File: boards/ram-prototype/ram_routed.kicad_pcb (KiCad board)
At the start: 4 copper layers, 159 x 77 mm, 512 parts, among them J1 PinHeader_1x16_P2\.54mm_Verti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, U1 DSBGA\-5_NumericPads, U10 DSBGA\-6_NumericPads, U100 DSBGA\-5_NumericPads, U101 DSBGA\-5_NumericPads, U102 DSBGA\-5_NumericPads, U103 DSBGA\-5_NumericPads, U104 DSBGA\-5_NumericPads, U105 DSBGA\-5_NumericPads, U106 DSBGA\-5_NumericPads, U107 DSBGA\-5_NumericPads, U108 DSBGA\-5_NumericPads, U109 DSBGA\-5_NumericPads, U11 DSBGA\-6_NumericPads, U110 DSBGA\-5_NumericPads, U111 DSBGA\-5_NumericPads, U112 DSBGA\-5_NumericPads, U113 DSBGA\-5_NumericPads, U114 DSBGA\-5_NumericPads, U115 DSBGA\-5_NumericPads, U116 DSBGA\-5_NumericPads, U117 DSBGA\-5_NumericPads, U118 DSBGA\-5_NumericPads, U119 DSBGA\-5_NumericPads, U12 DSBGA\-5_NumericPads, U120 DSBGA\-5_NumericPads, U121 DSBGA\-5_NumericPads, U122 DSBGA\-5_NumericPads, U123 DSBGA\-5_NumericPads, U124 DSBGA\-5_NumericPads, U125 DSBGA\-5_NumericPads, U126 DSBGA\-5_NumericPads, U127 DSBGA\-5_NumericPads, U128 DSBGA\-5_NumericPads, U129 DSBGA\-5_NumericPads, U13 DSBGA\-5_NumericPads, U130 DSBGA\-5_NumericPads, U131 DSBGA\-5_NumericPads, U132 DSBGA\-5_NumericPads, U133 DSBGA\-5_NumericPads, U134 DSBGA\-5_NumericPads, U135 DSBGA\-5_NumericPads, U136 DSBGA\-5_NumericPads, U137 DSBGA\-5_NumericPads, U138 DSBGA\-5_NumericPads, U139 DSBGA\-5_NumericPads, U14 DSBGA\-5_NumericPads, U140 DSBGA\-5_NumericPads, U141 DSBGA\-5_NumericPads, U142 DSBGA\-5_NumericPads, U143 DSBGA\-5_NumericPads, U144 DSBGA\-5_NumericPads, U145 DSBGA\-5_NumericPads, U146 DSBGA\-5_NumericPads, U147 DSBGA\-5_NumericPads, U148 DSBGA\-5_NumericPads, U149 DSBGA\-5_NumericPads, U15 DSBGA\-5_NumericPads, U150 DSBGA\-5_NumericPads, U151 DSBGA\-5_NumericPads, U152 DSBGA\-5_NumericPads, U153 DSBGA\-5_NumericPads, U154 DSBGA\-5_NumericPads, U155 DSBGA\-5_NumericPads, U156 DSBGA\-5_NumericPads, U157 DSBGA\-5_NumericPads, U158 DSBGA\-5_NumericPads, U159 DSBGA\-5_NumericPads, U16 DSBGA\-5_NumericPads, U160 DSBGA\-5_NumericPads, U161 DSBGA\-5_NumericPads, U17 DSBGA\-5_NumericPads, U18 DSBGA\-5_NumericPads, U19 DSBGA\-5_NumericPads, U2 DSBGA\-5_NumericPads, U20 DSBGA\-5_NumericPads, U21 DSBGA\-5_NumericPads, U22 DSBGA\-5_NumericPads, U23 DSBGA\-5_NumericPads, U24 DSBGA\-5_NumericPads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

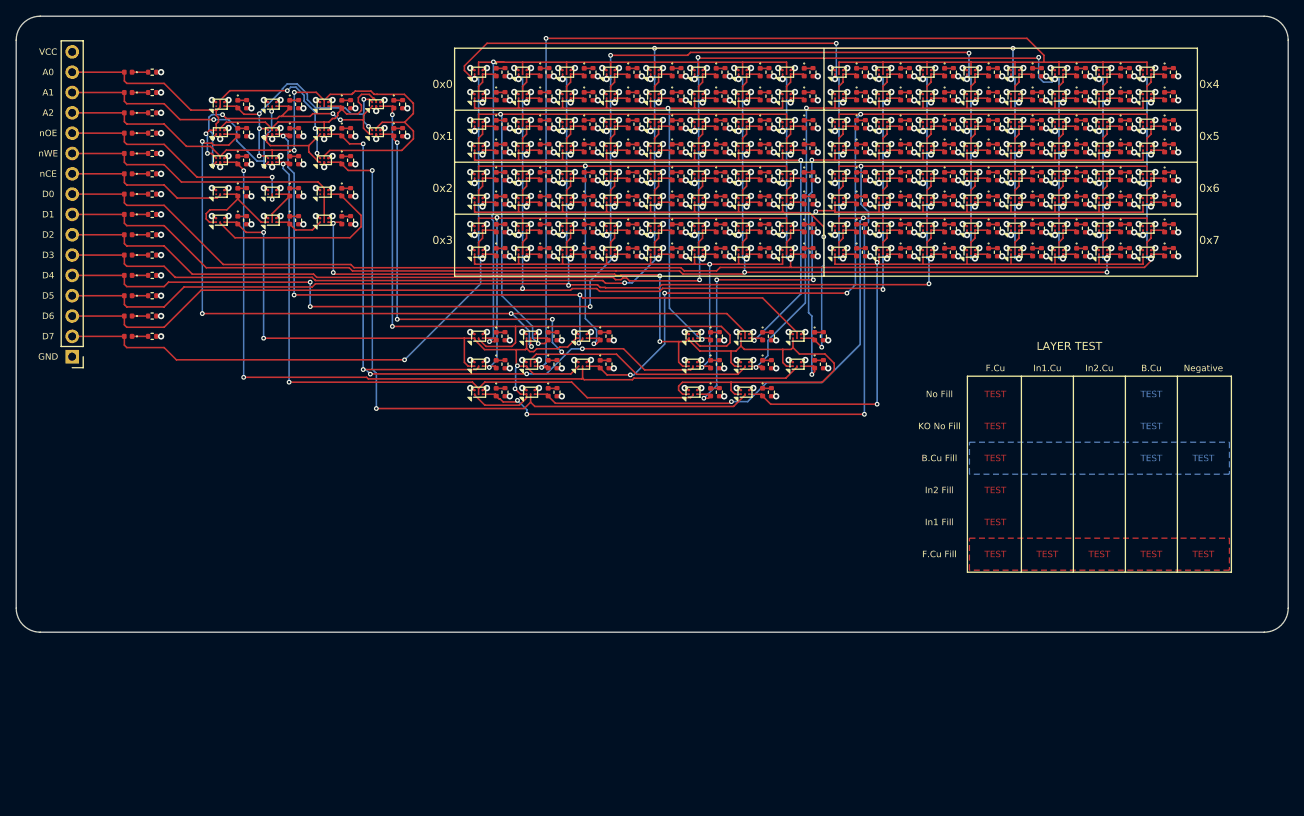
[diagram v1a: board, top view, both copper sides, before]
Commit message: flip resistor to the back
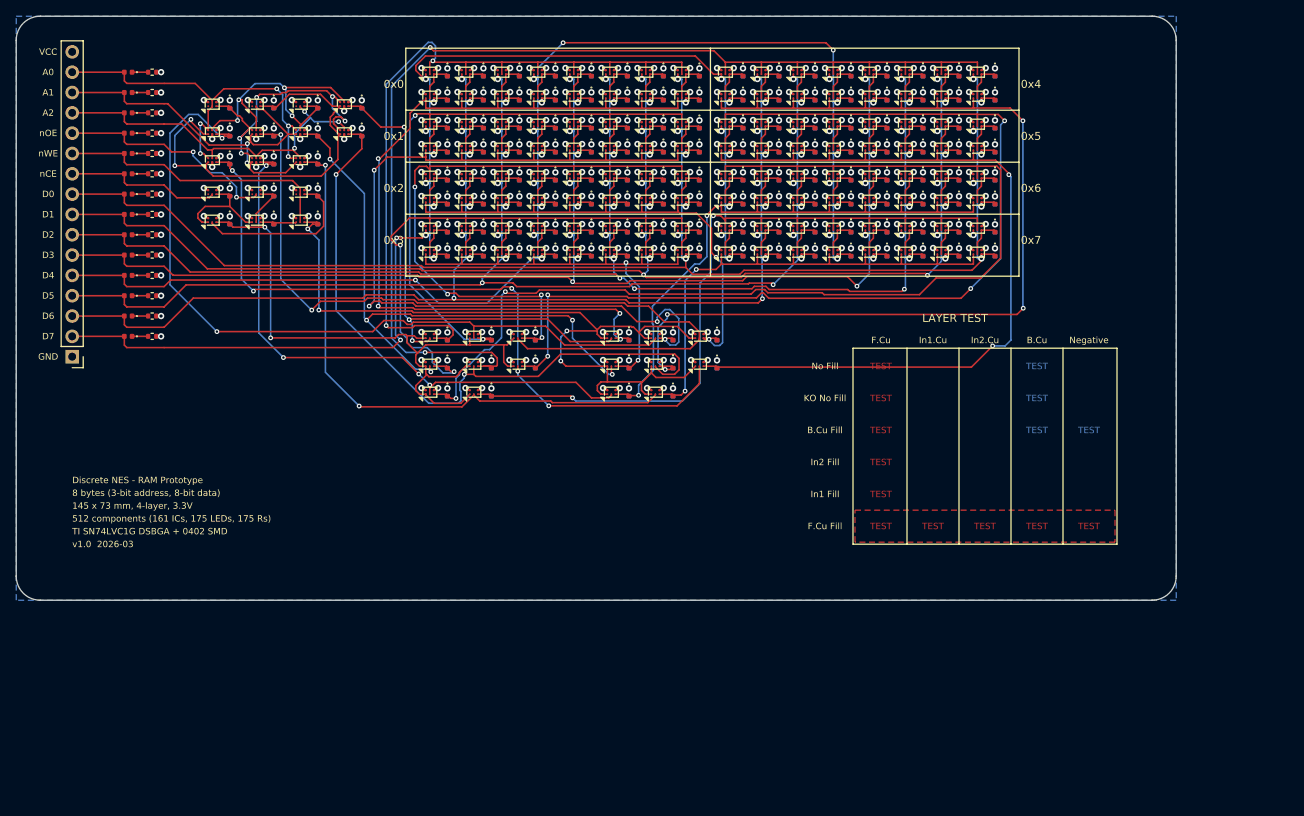
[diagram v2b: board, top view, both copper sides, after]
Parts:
- R100, R101, R102, R103, R104, R105, R106, R107, R108, R109, R110, R111, R112, R113, R114, R115, R116, R117, R118, R119, R120, R121, R122, R123, R124, R125, R126, R127, R128, R129, R130, R131, R132, R133, R134, R135, R136, R137, R138, R139, R140, R141, R142, R143, R144, R145, R146, R147, R148, R149, R15, R150, R151, R152, R153, R154, R155, R156, R157, R158, R159, R16, R160, R161, R162, R163, R164, R165, R166, R167, R168, R169, R17, R170, R171, R172, R173, R174, R175, R18, R19, R20, R21, R22, R23, R24, R25, R26, R27, R28, R29, R30, R31, R32, R33, R34, R35, R36, R37, R38, R39, R40, R41, R42, R43, R44, R45, R46, R47, R48, R49, R50, R51, R52, R53, R54, R55, R56, R57, R58, R59, R60, R61, R62, R63, R64, R65, R66, R67, R68, R69, R70, R71, R72, R73, R74, R75, R76, R77, R78, R79, R80, R81, R82, R83, R84, R85, R86, R87, R88, R89, R90, R91, R92, R93, R94, R95, R96, R97, R98, R99: moved to B.Cu
- moved R52 22.3 mm to (135.3, 20.0)
- moved R53 22.3 mm to (135.3, 26.5)
- moved R54 22.3 mm to (135.3, 33.0)
- moved R55 22.3 mm to (135.3, 39.5)
- moved R60 22.3 mm to (135.3, 23.0)
- moved R61 22.3 mm to (135.3, 29.5)
- moved R62 22.3 mm to (135.3, 36.0)
- moved R63 22.3 mm to (135.3, 42.5)
- moved R68 21.3 mm to (130.8, 20.0)
- moved R69 21.3 mm to (130.8, 26.5)
- moved R70 21.3 mm to (130.8, 33.0)
- moved R71 21.3 mm to (130.8, 39.5)
- moved R76 21.3 mm to (130.8, 23.0)
- moved R77 21.3 mm to (130.8, 29.5)
- moved R78 21.3 mm to (130.8, 36.0)
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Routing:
- net GND: track 202.2 -> 105.6 mm, vias 336 -> 175
- net /BUF_OE_4: track 89.8 -> 127.2 mm, vias 2 -> 4
- net /BUF_OE_1: track 78.1 -> 114.4 mm, vias 2 -> 4
- net /Address Decoder/A2: track 78.4 -> 45.6 mm, vias 2 -> 3
- net /BUF_OE_5: track 81.3 -> 107.6 mm
- net /BUF_OE_0: track 81.4 -> 106.7 mm, vias 2 -> 4
- net /Byte 5/WRITE_CLK: track 114.6 -> 135.7 mm
- net /Address Decoder/SEL0: track 85.5 -> 64.5 mm, vias 2 -> 3
- net /D0: track 218.3 -> 197.4 mm
- net /D3: track 205.8 -> 185.0 mm, vias 19 -> 18
- net /D4: track 204.5 -> 183.7 mm, vias 21 -> 19
- net /D1: track 213.5 -> 193.1 mm
- net /Byte 4/WRITE_CLK: track 158.5 -> 138.2 mm
- net /D2: track 211.7 -> 191.5 mm
- net /BUF_OE_7: track 83.1 -> 64.3 mm
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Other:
- board size 159 x 77 mm -> 145 x 73 mm
- board text added: "145 x 73 mm, 4-layer, 3.3V"
- board text added: "512 components (161 ICs, 175 LEDs, 175 Rs)"
- board text added: "8 bytes (3-bit address, 8-bit data)"
- board text added: "Discrete NES - RAM Prototype"
- board text added: "TI SN74LVC1G DSBGA + 0402 SMD"
- board text added: "v1.0 2026-03"

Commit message: Fix some layer issues
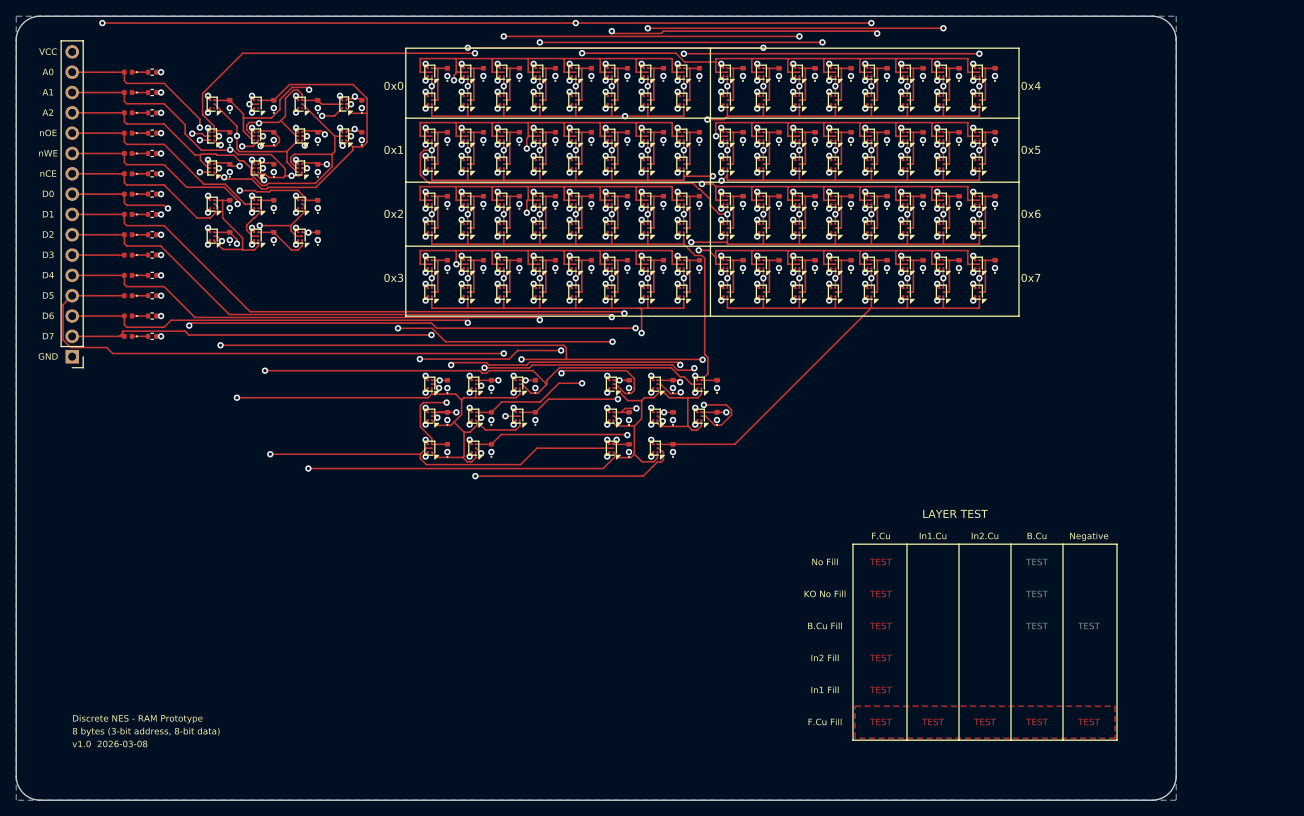
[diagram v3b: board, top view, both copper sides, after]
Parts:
- removed D112, D113, D114, D115, D116, D117, D118, D119, D120, D121, D122, D123, D124, D125, D126, D127, D128, D129, D130, D131, D132, D133, D134, D135, D136, D137, D138, D139, D140, D141, D142, D143, D144, D145, D146, D147, D148, D149, D150, D151, D152, D153, D154, D155, D156, D157, D158, D159, D160, D161, D162, D163, D164, D165, D166, D167, D168, D169, D170, D171, D172, D173, D174, D175: LED_0402_1005Metric, LED_SMD:LED_0402_1005Metric
- removed R112, R113, R114, R115, R116, R117, R118, R119, R120, R121, R122, R123, R124, R125, R126, R127, R128, R129, R130, R131, R132, R133, R134, R135, R136, R137, R138, R139, R140, R141, R142, R143, R144, R145, R146, R147, R148, R149, R150, R151, R152, R153, R154, R155, R156, R157, R158, R159, R160, R161, R162, R163, R164, R165, R166, R167, R168, R169, R170, R171, R172, R173, R174, R175: R_0402_1005Metric, Resistor_SMD:R_0402_1005Metric
- J1: moved to B.Cu
- moved D104 18.2 mm to (66.9, 20.0), turned to 90 degrees
- moved D108 18.2 mm to (103.8, 20.0), turned to 90 degrees
- moved R104 18.2 mm to (66.9, 20.0), turned to 90 degrees
- moved R108 18.2 mm to (103.8, 20.0), turned to 90 degrees
- moved D105 18.1 mm to (66.9, 28.0), turned to 90 degrees
- moved D107 18.1 mm to (66.9, 44.0), turned to 90 degrees
- moved D109 18.1 mm to (103.8, 28.0), turned to 90 degrees
- moved D111 18.1 mm to (103.8, 44.0), turned to 90 degrees
- moved R105 18.1 mm to (66.9, 28.0), turned to 90 degrees
- moved R107 18.1 mm to (66.9, 44.0), turned to 90 degrees
- moved R109 18.1 mm to (103.8, 28.0), turned to 90 degrees
- moved R111 18.1 mm to (103.8, 44.0), turned to 90 degrees
- moved D106 18.0 mm to (66.9, 36.0), turned to 90 degrees
- moved D110 18.0 mm to (103.8, 36.0), turned to 90 degrees
- moved R106 18.0 mm to (66.9, 36.0), turned to 90 degrees
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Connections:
- D104 pad 2: /D3 -> Net-(D104-A)
- D105 pad 2: /D3 -> Net-(D105-A)
- D106 pad 2: /D3 -> Net-(D106-A)
- D107 pad 2: /D3 -> Net-(D107-A)
- D108 pad 2: /D3 -> Net-(D108-A)
- D109 pad 2: /D3 -> Net-(D109-A)
- D110 pad 2: /D3 -> Net-(D110-A)
- D111 pad 2: /D3 -> Net-(D111-A)
- D56 pad 2: /D0 -> Net-(D56-A)
- D57 pad 2: /D0 -> Net-(D57-A)
- D58 pad 2: /D0 -> Net-(D58-A)
- D59 pad 2: /D0 -> Net-(D59-A)
- D60 pad 2: /D0 -> Net-(D60-A)
- D61 pad 2: /D0 -> Net-(D61-A)
- D62 pad 2: /D0 -> Net-(D62-A)
- D63 pad 2: /D0 -> Net-(D63-A)
- D72 pad 2: /D1 -> Net-(D72-A)
- D73 pad 2: /D1 -> Net-(D73-A)
- D74 pad 2: /D1 -> Net-(D74-A)
- D75 pad 2: /D1 -> Net-(D75-A)
- D76 pad 2: /D1 -> Net-(D76-A)
- D77 pad 2: /D1 -> Net-(D77-A)
- D78 pad 2: /D1 -> Net-(D78-A)
- D79 pad 2: /D1 -> Net-(D79-A)
- D88 pad 2: /D2 -> Net-(D88-A)
- D89 pad 2: /D2 -> Net-(D89-A)
- D90 pad 2: /D2 -> Net-(D90-A)
- D91 pad 2: /D2 -> Net-(D91-A)
- D92 pad 2: /D2 -> Net-(D92-A)
- D93 pad 2: /D2 -> Net-(D93-A)
- D94 pad 2: /D2 -> Net-(D94-A)
- D95 pad 2: /D2 -> Net-(D95-A)
- U100 pad 4: Net-(D114-A) -> Net-(D82-A)
- U101 pad 4: Net-(D115-A) -> Net-(D83-A)
- U102 pad 4: Net-(D116-A) -> Net-(D84-A)
- U103 pad 4: Net-(D117-A) -> Net-(D85-A)
- U104 pad 4: Net-(D118-A) -> Net-(D86-A)
- U105 pad 4: Net-(D119-A) -> Net-(D87-A)
- U106 pad 2: Net-(D112-A) -> Net-(D80-A)
- U107 pad 2: Net-(D113-A) -> Net-(D81-A)
- U108 pad 2: Net-(D114-A) -> Net-(D82-A)
- U109 pad 2: Net-(D115-A) -> Net-(D83-A)
- U110 pad 2: Net-(D116-A) -> Net-(D84-A)
- U111 pad 2: Net-(D117-A) -> Net-(D85-A)
- U112 pad 2: Net-(D118-A) -> Net-(D86-A)
- U113 pad 2: Net-(D119-A) -> Net-(D87-A)
- U114 pad 4: Net-(D128-A) -> Net-(D88-A)
- U115 pad 4: Net-(D129-A) -> Net-(D89-A)
- U116 pad 4: Net-(D130-A) -> Net-(D90-A)
- U117 pad 4: Net-(D131-A) -> Net-(D91-A)
- U118 pad 4: Net-(D132-A) -> Net-(D92-A)
- U119 pad 4: Net-(D133-A) -> Net-(D93-A)
- U120 pad 4: Net-(D134-A) -> Net-(D94-A)
- U121 pad 4: Net-(D135-A) -> Net-(D95-A)
- U122 pad 2: Net-(D128-A) -> Net-(D88-A)
- U123 pad 2: Net-(D129-A) -> Net-(D89-A)
- U124 pad 2: Net-(D130-A) -> Net-(D90-A)
- U125 pad 2: Net-(D131-A) -> Net-(D91-A)
- U126 pad 2: Net-(D132-A) -> Net-(D92-A)
- U127 pad 2: Net-(D133-A) -> Net-(D93-A)
- U128 pad 2: Net-(D134-A) -> Net-(D94-A)
- U129 pad 2: Net-(D135-A) -> Net-(D95-A)
- U130 pad 4: Net-(D144-A) -> Net-(D96-A)
- U131 pad 4: Net-(D145-A) -> Net-(D97-A)
- U132 pad 4: Net-(D146-A) -> Net-(D98-A)
- U133 pad 4: Net-(D147-A) -> Net-(D99-A)
- U134 pad 4: Net-(D148-A) -> Net-(D100-A)
- U135 pad 4: Net-(D149-A) -> Net-(D101-A)
- U136 pad 4: Net-(D150-A) -> Net-(D102-A)
- U137 pad 4: Net-(D151-A) -> Net-(D103-A)
- U138 pad 2: Net-(D144-A) -> Net-(D96-A)
- U139 pad 2: Net-(D145-A) -> Net-(D97-A)
- U140 pad 2: Net-(D146-A) -> Net-(D98-A)
- U141 pad 2: Net-(D147-A) -> Net-(D99-A)
- U142 pad 2: Net-(D148-A) -> Net-(D100-A)
- U143 pad 2: Net-(D149-A) -> Net-(D101-A)
- U144 pad 2: Net-(D150-A) -> Net-(D102-A)
- U145 pad 2: Net-(D151-A) -> Net-(D103-A)
- U146 pad 4: Net-(D160-A) -> Net-(D104-A)
- U147 pad 4: Net-(D161-A) -> Net-(D105-A)
- U148 pad 4: Net-(D162-A) -> Net-(D106-A)
- U149 pad 4: Net-(D163-A) -> Net-(D107-A)
- U150 pad 4: Net-(D164-A) -> Net-(D108-A)
- U151 pad 4: Net-(D165-A) -> Net-(D109-A)
- U152 pad 4: Net-(D166-A) -> Net-(D110-A)
- U153 pad 4: Net-(D167-A) -> Net-(D111-A)
- U154 pad 2: Net-(D160-A) -> Net-(D104-A)
- U155 pad 2: Net-(D161-A) -> Net-(D105-A)
- U156 pad 2: Net-(D162-A) -> Net-(D106-A)
- U157 pad 2: Net-(D163-A) -> Net-(D107-A)
- U158 pad 2: Net-(D164-A) -> Net-(D108-A)
- U159 pad 2: Net-(D165-A) -> Net-(D109-A)
- U160 pad 2: Net-(D166-A) -> Net-(D110-A)
- U161 pad 2: Net-(D167-A) -> Net-(D111-A)
- U50 pad 4: Net-(D64-A) -> Net-(D56-A)
- U51 pad 4: Net-(D65-A) -> Net-(D57-A)
- U52 pad 4: Net-(D66-A) -> Net-(D58-A)
- U53 pad 4: Net-(D67-A) -> Net-(D59-A)
- U54 pad 4: Net-(D68-A) -> Net-(D60-A)
- U55 pad 4: Net-(D69-A) -> Net-(D61-A)
- U56 pad 4: Net-(D70-A) -> Net-(D62-A)
- U57 pad 4: Net-(D71-A) -> Net-(D63-A)
- U58 pad 2: Net-(D64-A) -> Net-(D56-A)
- U59 pad 2: Net-(D65-A) -> Net-(D57-A)
- U60 pad 2: Net-(D66-A) -> Net-(D58-A)
- U61 pad 2: Net-(D67-A) -> Net-(D59-A)
- U62 pad 2: Net-(D68-A) -> Net-(D60-A)
- U63 pad 2: Net-(D69-A) -> Net-(D61-A)
- U64 pad 2: Net-(D70-A) -> Net-(D62-A)
- U65 pad 2: Net-(D71-A) -> Net-(D63-A)
- U66 pad 4: Net-(D80-A) -> Net-(D64-A)
- U67 pad 4: Net-(D81-A) -> Net-(D65-A)
- U68 pad 4: Net-(D82-A) -> Net-(D66-A)
- U69 pad 4: Net-(D83-A) -> Net-(D67-A)
- U70 pad 4: Net-(D84-A) -> Net-(D68-A)
- U71 pad 4: Net-(D85-A) -> Net-(D69-A)
- U72 pad 4: Net-(D86-A) -> Net-(D70-A)
- U73 pad 4: Net-(D87-A) -> Net-(D71-A)
- U74 pad 2: Net-(D80-A) -> Net-(D64-A)
- U75 pad 2: Net-(D81-A) -> Net-(D65-A)
- U76 pad 2: Net-(D82-A) -> Net-(D66-A)
- U77 pad 2: Net-(D83-A) -> Net-(D67-A)
- U78 pad 2: Net-(D84-A) -> Net-(D68-A)
- U79 pad 2: Net-(D85-A) -> Net-(D69-A)
- U80 pad 2: Net-(D86-A) -> Net-(D70-A)
- U81 pad 2: Net-(D87-A) -> Net-(D71-A)
- U82 pad 4: Net-(D96-A) -> Net-(D72-A)
- U83 pad 4: Net-(D97-A) -> Net-(D73-A)
- U84 pad 4: Net-(D98-A) -> Net-(D74-A)
- U85 pad 4: Net-(D99-A) -> Net-(D75-A)
- U86 pad 4: Net-(D100-A) -> Net-(D76-A)
- U87 pad 4: Net-(D101-A) -> Net-(D77-A)
- U88 pad 4: Net-(D102-A) -> Net-(D78-A)
- U89 pad 4: Net-(D103-A) -> Net-(D79-A)
- U90 pad 2: Net-(D96-A) -> Net-(D72-A)
- U91 pad 2: Net-(D97-A) -> Net-(D73-A)
- U92 pad 2: Net-(D98-A) -> Net-(D74-A)
- U93 pad 2: Net-(D99-A) -> Net-(D75-A)
- U94 pad 2: Net-(D100-A) -> Net-(D76-A)
- U95 pad 2: Net-(D101-A) -> Net-(D77-A)
- U96 pad 2: Net-(D102-A) -> Net-(D78-A)
- U97 pad 2: Net-(D103-A) -> Net-(D79-A)
- U98 pad 4: Net-(D112-A) -> Net-(D80-A)
- U99 pad 4: Net-(D113-A) -> Net-(D81-A)
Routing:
- net /BUF_OE_4: track 127.2 -> 87.0 mm, vias 4 -> 2
- net /BUF_OE_1: track 114.4 -> 77.7 mm, vias 4 -> 2
- net /D3: track 185.0 -> 217.0 mm, vias 18 -> 11
- net /BUF_OE_5: track 107.6 -> 77.5 mm
- net /Address Decoder/SEL5: track 90.9 -> 119.2 mm, vias 5 -> 6
- net /BUF_OE_0: track 106.7 -> 78.9 mm, vias 4 -> 2
- net /Address Decoder/SEL1: track 97.7 -> 120.5 mm, vias 2 -> 5
- net /D5: track 176.1 -> 195.1 mm, vias 18 -> 11
- net /Address Decoder/SEL0: track 64.5 -> 80.5 mm, vias 3 -> 5
- net /Byte 6/WRITE_CLK: track 141.9 -> 127.7 mm, vias 2 -> 4
- net /Address Decoder/A2: track 45.6 -> 58.8 mm, vias 3 -> 0
- net /Address Decoder/SEL6: track 73.4 -> 86.4 mm, vias 4 -> 2
- net /BUF_OE_7: track 64.3 -> 77.3 mm, vias 2 -> 0
- net /D7: track 178.3 -> 166.3 mm, vias 18 -> 9
- net /Control Logic/READ_EN: track 102.6 -> 113.0 mm, vias 4 -> 2
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- removed copper zone on In1.Cu, net GND
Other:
- board size 145 x 73 mm -> 145 x 98 mm
- board text added: "v1.0 2026-03-08"
- board text removed: "145 x 73 mm, 4-layer, 3.3V"
- board text removed: "512 components (161 ICs, 175 LEDs, 175 Rs)"
- board text removed: "TI SN74LVC1G DSBGA + 0402 SMD"
- board text removed: "v1.0 2026-03"
